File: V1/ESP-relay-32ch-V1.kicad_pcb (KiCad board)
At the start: 2 copper layers, 148 x 67.8 mm, 576 parts, among them J1 Conn_01x08, J10 USB, J11 ETHERNET, J2 Conn_01x08, J3 Conn_01x08, J4 Conn_01x08, J5 Conn_01x08, J6 Conn_01x08, J7 Conn_01x08, J8 Conn_01x08, J9 VIN, Q1 WPM2015-3/TR, Q10 MMBT2222A/SOT-23-3, Q11 MMBT2222A/SOT-23-3, Q12 MMBT2222A/SOT-23-3, Q13 MMBT2222A/SOT-23-3, Q14 MMBT2222A/SOT-23-3, Q15 MMBT2222A/SOT-23-3, Q16 MMBT2222A/SOT-23-3, Q17 MMBT2222A/SOT-23-3, Q18 MMBT2222A/SOT-23-3, Q19 MMBT2222A/SOT-23-3, Q2 LMUN2211LT1G, Q20 MMBT2222A/SOT-23-3, Q21 MMBT2222A/SOT-23-3, Q22 MMBT2222A/SOT-23-3, Q23 MMBT2222A/SOT-23-3, Q24 MMBT2222A/SOT-23-3, Q25 MMBT2222A/SOT-23-3, Q26 MMBT2222A/SOT-23-3, Q27 MMBT2222A/SOT-23-3, Q28 MMBT2222A/SOT-23-3, Q29 MMBT2222A/SOT-23-3, Q3 UMH3N, Q30 MMBT2222A/SOT-23-3, Q31 MMBT2222A/SOT-23-3, Q32 MMBT2222A/SOT-23-3, Q33 MMBT2222A/SOT-23-3, Q34 MMBT2222A/SOT-23-3, Q35 MMBT2222A/SOT-23-3, Q4 MMBT2222A/SOT-23-3, Q5 MMBT2222A/SOT-23-3, Q6 MMBT2222A/SOT-23-3, Q7 MMBT2222A/SOT-23-3, Q8 MMBT2222A/SOT-23-3, Q9 MMBT2222A/SOT-23-3, SW1 RESET, U1 SY8089A1AAC, U10 LTV-817S, U11 LTV-817S, U12 LTV-817S, U13 LTV-817S, U14 LTV-817S, U15 LTV-817S, U16 LTV-817S, U17 LTV-817S, U18 LTV-817S, U19 LTV-817S, U2 TX4138, U20 LTV-817S, U21 LTV-817S, U22 LTV-817S, U23 LTV-817S, U24 LTV-817S, U25 LTV-817S, U26 LTV-817S, U27 LTV-817S, U28 LTV-817S, U29 LTV-817S, U3 CH340C, U30 LTV-817S, U31 LTV-817S, U32 LTV-817S, U33 LTV-817S, U34 LTV-817S, U35 LTV-817S, U36 LTV-817S, U37 LTV-817S, U38 LTV-817S, U39 LTV-817S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

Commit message: Dev
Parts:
- removed the C11 at (94.6, 107.6)
- removed the C11 at (162.6, 81.4)
- removed the C12 at (162.6, 77.8)
- removed the C12 at (94.6, 101.3)
- removed the C13 at (186.1, 66.8)
- removed the C13 at (94.6, 94.9)
- removed the C14 at (184.2, 83.8)
- removed the C14 at (94.6, 88.6)
- removed the C15 at (172.5, 88.4)
- removed the C15 at (94.6, 82.2)
- removed the C16 at (198.8, 101.1)
- removed the C16 at (94.6, 75.9)
- removed the C17 at (113.7, 107.6)
- removed the C17 at (204.5, 96.7)
- removed the C18 at (113.7, 101.3)
- removed the C18 at (200.0, 100.8)
- removed the C19 at (193.4, 93.2)
- removed the C19 at (113.7, 94.9)
- removed the C20 at (201.5, 91.2)
- removed the C20 at (113.7, 88.6)
- removed the C21 at (191.3, 97.0)
- removed the C21 at (113.7, 82.2)
- removed the C22 at (113.7, 75.9)
- removed the C22 at (192.5, 97.0)
- removed the C23 at (262.1, 90.8)
- removed the C23 at (132.7, 107.6)
- removed the C25 at (262.1, 96.8)
- removed the C25 at (132.7, 94.9)
- removed the C26 at (132.7, 88.6)
- removed the C26 at (262.1, 99.9)
- removed the D10 at (279.7, 98.4)
- removed the D10 at (94.0, 114.8)
- removed the D11 at (298.6, 70.8)
- removed the D11 at (97.2, 94.1)
- removed the D12 at (298.6, 74.0)
- removed the D12 at (97.8, 114.8)
- removed the D13 at (298.6, 77.3)
- removed the D13 at (97.2, 87.8)
- removed the D14 at (101.6, 114.8)
- removed the D14 at (298.6, 80.5)
- removed the D15 at (279.7, 101.0)
- removed the D15 at (97.2, 81.4)
- removed the D16 at (279.7, 103.6)
- removed the D16 at (105.4, 114.8)
- removed the D17 at (283.8, 90.6)
- removed the D17 at (97.2, 75.1)
- removed the D18 at (109.2, 114.8)
- removed the D18 at (283.8, 93.2)
- removed the D19 at (116.2, 106.8)
- removed the D19 at (298.6, 83.8)
- removed the D20 at (113.0, 114.8)
- removed the D20 at (298.6, 87.0)
- removed the D21 at (304.9, 70.8)
- removed the D21 at (116.2, 100.5)
- removed the D22 at (116.8, 114.8)
- removed the D22 at (304.9, 74.0)
- removed the D23 at (116.2, 94.1)
- removed the D23 at (283.8, 95.8)
- removed the D24 at (283.8, 98.4)
- removed the D24 at (120.7, 114.8)
- removed the D25 at (116.2, 87.8)
- removed the D25 at (283.8, 101.0)
- removed the D26 at (124.5, 114.8)
- removed the D26 at (283.8, 103.6)
- removed the D27 at (304.9, 77.3)
- removed the D27 at (116.2, 81.4)
- removed the D28 at (128.3, 114.8)
- removed the D28 at (304.9, 80.5)
- removed the D29 at (304.9, 83.8)
- removed the D29 at (116.2, 75.1)
- removed the D30 at (132.1, 114.8)
- removed the D30 at (304.9, 87.0)
- removed the D31 at (135.3, 106.8)
- removed the D31 at (287.8, 90.6)
- removed the D32 at (287.8, 93.2)
- removed the D32 at (135.9, 114.8)
- removed the D33 at (135.3, 100.5)
- removed the D33 at (287.8, 95.8)
- removed the D34 at (287.8, 98.4)
- removed the D34 at (139.7, 114.8)
- removed the D35 at (135.3, 94.1)
- removed the D35 at (311.3, 70.8)
- removed the D36 at (311.3, 74.0)
- removed the D36 at (143.5, 114.8)
- removed the D37 at (135.3, 87.8)
- removed the D37 at (311.3, 77.3)
- removed the D6 at (160.0, 86.7)
- removed the D6 at (86.4, 114.8)
- removed the D7 at (97.2, 106.8)
- removed the D7 at (279.7, 90.6)
- removed the D8 at (279.7, 93.2)
- removed the D8 at (90.2, 114.8)
- removed the D9 at (97.2, 100.5)
- removed the D9 at (279.7, 95.8)
- removed the R10 at (86.4, 117.9)
- removed the R10 at (188.0, 68.1)
- removed the R11 at (207.3, 87.6)
- removed the R11 at (88.3, 117.3)
- removed the R12 at (110.5, 105.5)
- removed the R12 at (188.2, 83.1)
- removed the R13 at (90.2, 117.9)
- removed the R13 at (186.9, 75.4)
- removed the R14 at (188.2, 76.2)
- removed the R14 at (92.1, 117.3)
- removed the R15 at (194.9, 100.8)
- removed the R15 at (110.5, 99.2)
- removed the R16 at (183.9, 89.9)
- removed the R16 at (94.0, 117.9)
- removed the R17 at (193.4, 94.5)
- removed the R17 at (95.9, 117.3)
- removed the R18 at (196.2, 100.8)
- removed the R18 at (110.5, 92.8)
- removed the R19 at (197.5, 100.8)
- removed the R19 at (97.8, 117.9)
- removed the R20 at (193.7, 100.8)
- removed the R20 at (99.7, 117.3)
- removed the R21 at (192.4, 100.8)
- removed the R21 at (110.5, 86.5)
- removed the R22 at (203.8, 100.8)
- removed the R22 at (101.6, 117.9)
- removed the R23 at (103.5, 117.3)
- removed the R23 at (201.3, 100.8)
- removed the R24 at (110.5, 80.1)
- removed the R24 at (203.2, 96.4)
- removed the R25 at (202.6, 100.8)
- removed the R25 at (105.4, 117.9)
- removed the R26 at (193.4, 91.9)
- removed the R26 at (107.3, 117.3)
- removed the R27 at (197.1, 89.4)
- removed the R27 at (110.5, 73.8)
- removed the R28 at (199.0, 91.2)
- removed the R28 at (109.2, 117.9)
- removed the R29 at (111.1, 117.3)
- removed the R29 at (193.4, 90.7)
- removed the R30 at (193.4, 89.4)
- removed the R30 at (129.5, 105.5)
- removed the R31 at (317.9, 62.5)
- removed the R31 at (113.0, 117.9)
- removed the R32 at (317.9, 64.5)
- removed the R32 at (114.9, 117.3)
- removed the R33 at (129.5, 99.2)
- removed the R33 at (317.9, 66.5)
- removed the R34 at (317.9, 68.4)
- removed the R34 at (116.8, 117.9)
- removed the R35 at (118.7, 117.3)
- removed the R35 at (291.8, 90.6)
- removed the R36 at (291.8, 93.1)
- removed the R36 at (129.5, 92.8)
- removed the R37 at (291.8, 95.6)
- removed the R37 at (120.7, 117.9)
- removed the R38 at (122.6, 117.3)
- removed the R38 at (291.8, 98.1)
- removed the R39 at (129.5, 86.5)
- removed the R39 at (298.2, 51.1)
- removed the R40 at (298.2, 54.4)
- removed the R40 at (124.5, 117.9)
- removed the R41 at (298.2, 57.6)
- removed the R41 at (126.4, 117.3)
- removed the R42 at (298.2, 60.9)
- removed the R42 at (129.5, 80.1)
- removed the R43 at (128.3, 117.9)
- removed the R43 at (303.3, 90.3)
- removed the R44 at (130.2, 117.3)
- removed the R44 at (303.3, 92.3)
- removed the R45 at (303.3, 94.3)
- removed the R45 at (130.1, 74.3)
- removed the R46 at (303.3, 96.3)
- removed the R46 at (132.1, 117.9)
- removed the R47 at (291.8, 100.6)
- removed the R47 at (134.0, 117.3)
- removed the R48 at (148.6, 105.5)
- removed the R48 at (291.8, 103.1)
- removed the R49 at (135.9, 117.9)
- removed the R49 at (295.8, 90.6)
- removed the R50 at (295.8, 93.1)
- removed the R50 at (137.8, 117.3)
- removed the R51 at (298.2, 64.2)
- removed the R51 at (148.6, 97.9)
- removed the R52 at (139.7, 117.9)
- removed the R52 at (298.2, 67.5)
- removed the R53 at (141.6, 117.3)
- removed the R53 at (303.8, 51.1)
- removed the R54 at (303.8, 54.4)
- removed the R54 at (148.6, 92.8)
- removed the R55 at (306.2, 90.3)
- removed the R55 at (143.5, 117.9)
- removed the R56 at (306.2, 92.3)
- removed the R56 at (145.4, 117.3)
- removed the R57 at (148.6, 86.5)
- removed the R57 at (306.2, 94.3)
- removed the U10 at (123.2, 101.0)
- removed the U10 at (265.8, 52.8)
- removed the U11 at (123.2, 94.6)
- removed the U11 at (265.8, 59.4)
- removed the U12 at (265.8, 66.0)
- removed the U12 at (123.2, 88.3)
- removed the U13 at (123.2, 81.9)
- removed the U13 at (265.8, 72.7)
- removed the U14 at (265.8, 79.3)
- removed the U14 at (123.2, 75.6)
- removed U18, U19, U20, U21, U22, U23, U24, U25, U26, U27, U28, U29, U30, U31, U32, U33, U34, U35, U36, U37, U38, U39, U40, U41: LTV-817S, Tales:SMDIP-4_W9.53mm
- removed the U9 at (353.4, 55.5)
- removed the U9 at (123.2, 107.3)
- added C11: 10uF/6,3V/0603, Tales:C_0603_1608Metric, F.Cu at (156.8, 30.1)
- added C12: 0,1uF/50V/0805, Tales:C_0805_2012Metric, F.Cu at (157.0, 35.4)
- added C13: 1uF/10V/0603, Tales:C_0603_1608Metric, F.Cu at (156.8, 32.7)
- added C14: 1nF/2kV/1206, Tales:C_1206_3216Metric, F.Cu at (122.4, 43.0)
- added C15: 0,1uF/16V/0402, Tales:C_0402_1005Metric, F.Cu at (122.7, 18.4)
- added C16: 10uF/6,3V/0603, Tales:C_0603_1608Metric, F.Cu at (123.2, 30.5)
- added C17: 10uF/6,3V/0603, Tales:C_0603_1608Metric, F.Cu at (123.2, 33.0)
- added C18: 0,1uF/16V/0402, Tales:C_0402_1005Metric, F.Cu at (122.7, 20.4)
- added C19: 0,1uF/16V/0402, Tales:C_0402_1005Metric, F.Cu at (122.7, 22.4)
- added C20: 0,1uF/16V/0402, Tales:C_0402_1005Metric, F.Cu at (122.7, 24.4)
- added C21: 1uF/6,3V/0402, Tales:C_0402_1005Metric, F.Cu at (122.7, 26.3)
- added C22: 470pF/16V/0402, Tales:C_0402_1005Metric, F.Cu at (122.7, 28.3)
- added C23: 33nF/50V/0805, Tales:C_0805_2012Metric, F.Cu at (71.1, 105.7)
- added C25: 33nF/50V/0805, Tales:C_0805_2012Metric, F.Cu at (76.2, 105.7)
- added C26: 33nF/50V/0805, Tales:C_0805_2012Metric, F.Cu at (78.7, 105.7)
- added D10: BLUE/0603, Tales:LED_0603_1608Metric, F.Cu at (78.7, 117.0)
- added D11: 9V1/500mW, Tales:D_MiniMELF, F.Cu at (71.1, 100.8)
- added D12: 9V1/500mW, Tales:D_MiniMELF, F.Cu at (73.7, 100.8)
- added D13: 9V1/500mW, Tales:D_MiniMELF, F.Cu at (76.2, 100.8)
- added D14: 9V1/500mW, Tales:D_MiniMELF, F.Cu at (78.7, 100.8)
- added D15: BLUE/0603, Tales:LED_0603_1608Metric, F.Cu at (81.3, 117.0)
- added D16: BLUE/0603, Tales:LED_0603_1608Metric, F.Cu at (83.8, 117.0)
- added D17: BLUE/0603, Tales:LED_0603_1608Metric, F.Cu at (86.4, 117.0)
- added D18: BLUE/0603, Tales:LED_0603_1608Metric, F.Cu at (88.9, 117.0)
- added D19: 9V1/500mW, Tales:D_MiniMELF, F.Cu at (81.3, 100.8)
- added D20: 9V1/500mW, Tales:D_MiniMELF, F.Cu at (83.8, 100.8)
- added D21: 9V1/500mW, Tales:D_MiniMELF, F.Cu at (86.4, 100.8)
- added D22: 9V1/500mW, Tales:D_MiniMELF, F.Cu at (88.9, 100.8)
- added D23: BLUE/0603, Tales:LED_0603_1608Metric, F.Cu at (94.0, 117.0)
- added D24: BLUE/0603, Tales:LED_0603_1608Metric, F.Cu at (96.5, 117.0)
- added D25: BLUE/0603, Tales:LED_0603_1608Metric, F.Cu at (99.1, 117.0)
- added D26: BLUE/0603, Tales:LED_0603_1608Metric, F.Cu at (101.6, 117.0)
- added D27: 9V1/500mW, Tales:D_MiniMELF, F.Cu at (94.0, 100.8)
- added D28: 9V1/500mW, Tales:D_MiniMELF, F.Cu at (96.5, 100.8)
- added D29: 9V1/500mW, Tales:D_MiniMELF, F.Cu at (99.1, 100.8)
- added D30: 9V1/500mW, Tales:D_MiniMELF, F.Cu at (101.6, 100.8)
- added D31: BLUE/0603, Tales:LED_0603_1608Metric, F.Cu at (104.1, 117.0)
- added D32: BLUE/0603, Tales:LED_0603_1608Metric, F.Cu at (106.7, 117.0)
- added D33: BLUE/0603, Tales:LED_0603_1608Metric, F.Cu at (109.2, 117.0)
- added D34: BLUE/0603, Tales:LED_0603_1608Metric, F.Cu at (111.8, 117.0)
- added D35: 9V1/500mW, Tales:D_MiniMELF, F.Cu at (104.1, 100.8)
- added D36: 9V1/500mW, Tales:D_MiniMELF, F.Cu at (106.7, 100.8)
- added D37: 9V1/500mW, Tales:D_MiniMELF, F.Cu at (109.2, 100.8)
- added D6: ESDS314DBV, Package_TO_SOT_SMD:SOT-23-5, F.Cu at (122.2, 46.9)
- added D7: BLUE/0603, Tales:LED_0603_1608Metric, F.Cu at (71.1, 117.0)
- added D8: BLUE/0603, Tales:LED_0603_1608Metric, F.Cu at (73.7, 117.0)
- added D9: BLUE/0603, Tales:LED_0603_1608Metric, F.Cu at (76.2, 117.0)
- added R10: 10k/62,5mW/0402, Tales:R_0402_1005Metric, F.Cu at (153.3, 29.9)
- added R11: 10k/62,5mW/0402, Tales:R_0402_1005Metric, F.Cu at (153.3, 31.9)
- added R12: 10k/62,5mW/0402, Tales:R_0402_1005Metric, F.Cu at (153.3, 33.9)
- added R13: 3k3/62,5mW/0402, Tales:R_0402_1005Metric, F.Cu at (153.3, 35.9)
- added R14: 3k3/62,5mW/0402, Tales:R_0402_1005Metric, F.Cu at (153.3, 37.8)
- added R15: 3k3/62,5mW/0402, Tales:R_0402_1005Metric, F.Cu at (102.1, 42.3)
- added R16: 330R/62,5mW/0402, Tales:R_0402_1005Metric, F.Cu at (102.1, 44.3)
- added R17: 330R/62,5mW/0402, Tales:R_0402_1005Metric, F.Cu at (102.1, 46.3)
- added R18: 3k3/62,5mW/0402, Tales:R_0402_1005Metric, F.Cu at (102.1, 48.3)
- added R19: 3k3/62,5mW/0402, Tales:R_0402_1005Metric, F.Cu at (105.1, 42.3)
- added R20: 3k3/62,5mW/0402, Tales:R_0402_1005Metric, F.Cu at (105.1, 44.3)
- added R21: 3k3/62,5mW/0402, Tales:R_0402_1005Metric, F.Cu at (105.1, 46.3)
- added R22: 3k3/62,5mW/0402, Tales:R_0402_1005Metric, F.Cu at (105.1, 48.3)
- added R23: 3k3/62,5mW/0402, Tales:R_0402_1005Metric, F.Cu at (108.0, 42.3)
- added R24: 10k/62,5mW/0402, Tales:R_0402_1005Metric, F.Cu at (108.0, 44.3)
- added R25: 3k3/62,5mW/0402, Tales:R_0402_1005Metric, F.Cu at (108.0, 46.3)
- added R26: 12,1k/62,5mW/0402, Tales:R_0402_1005Metric, F.Cu at (108.0, 48.3)
- added R27: 49,9R/62,5mW/0402, Tales:R_0402_1005Metric, F.Cu at (110.9, 42.3)
- added R28: 49,9R/62,5mW/0402, Tales:R_0402_1005Metric, F.Cu at (110.9, 44.3)
- added R29: 49,9R/62,5mW/0402, Tales:R_0402_1005Metric, F.Cu at (110.9, 46.3)
- added R30: 49,9R/62,5mW/0402, Tales:R_0402_1005Metric, F.Cu at (110.9, 48.3)
- added R31: 1k/62,5mW/0402, Tales:R_0402_1005Metric, F.Cu at (179.8, 32.1)
- added R32: 1k/62,5mW/0402, Tales:R_0402_1005Metric, F.Cu at (179.8, 34.1)
- added R33: 1k/62,5mW/0402, Tales:R_0402_1005Metric, F.Cu at (179.8, 36.1)
- added R34: 1k/62,5mW/0402, Tales:R_0402_1005Metric, F.Cu at (179.8, 38.1)
- added R35: 5,6k/0,1W/0603, Tales:R_0603_1608Metric, F.Cu at (71.1, 113.9)
- added R36: 5,6k/0,1W/0603, Tales:R_0603_1608Metric, F.Cu at (73.7, 113.9)
- added R37: 5,6k/0,1W/0603, Tales:R_0603_1608Metric, F.Cu at (76.2, 113.9)
- added R38: 5,6k/0,1W/0603, Tales:R_0603_1608Metric, F.Cu at (78.7, 113.9)
- added R39: 1k2/0,250W/1206, Tales:R_1206_3216Metric, F.Cu at (71.1, 110.0)
- added R40: 1k2/0,250W/1206, Tales:R_1206_3216Metric, F.Cu at (73.7, 110.0)
- added R41: 1k2/0,250W/1206, Tales:R_1206_3216Metric, F.Cu at (76.2, 110.0)
- added R42: 1k2/0,250W/1206, Tales:R_1206_3216Metric, F.Cu at (78.7, 110.0)
- added R43: 3k3/62,5mW/0402, Tales:R_0402_1005Metric, F.Cu at (125.7, 130.1)
- added R44: 3k3/62,5mW/0402, Tales:R_0402_1005Metric, F.Cu at (127.0, 130.1)
- added R45: 3k3/62,5mW/0402, Tales:R_0402_1005Metric, F.Cu at (127.0, 124.0)
- added R46: 3k3/62,5mW/0402, Tales:R_0402_1005Metric, F.Cu at (125.7, 124.0)
- added R47: 5,6k/0,1W/0603, Tales:R_0603_1608Metric, F.Cu at (81.3, 113.9)
- added R48: 5,6k/0,1W/0603, Tales:R_0603_1608Metric, F.Cu at (83.8, 113.9)
- added R49: 5,6k/0,1W/0603, Tales:R_0603_1608Metric, F.Cu at (86.4, 113.9)
- added R50: 5,6k/0,1W/0603, Tales:R_0603_1608Metric, F.Cu at (88.9, 113.9)
- added R51: 1k2/0,250W/1206, Tales:R_1206_3216Metric, F.Cu at (81.3, 110.0)
- added R52: 1k2/0,250W/1206, Tales:R_1206_3216Metric, F.Cu at (83.8, 110.0)
- added R53: 1k2/0,250W/1206, Tales:R_1206_3216Metric, F.Cu at (86.4, 110.0)
- added R54: 1k2/0,250W/1206, Tales:R_1206_3216Metric, F.Cu at (88.9, 110.0)
- added R55: 3k3/62,5mW/0402, Tales:R_0402_1005Metric, F.Cu at (125.7, 121.8)
- added R56: 3k3/62,5mW/0402, Tales:R_0402_1005Metric, F.Cu at (127.0, 121.8)
- added R57: 3k3/62,5mW/0402, Tales:R_0402_1005Metric, F.Cu at (127.0, 115.7)
- added U10: OR-3H4-4, Package_SO:SOP-16_4.4x10.4mm_P1.27mm, F.Cu at (119.4, 127.0)
- added U11: OR-3H4-4, Package_SO:SOP-16_4.4x10.4mm_P1.27mm, F.Cu at (119.4, 118.8)
- added U12: OR-3H4-4, Package_SO:SOP-16_4.4x10.4mm_P1.27mm, F.Cu at (119.4, 110.5)
- added U13: OR-3H4-4, Package_SO:SOP-16_4.4x10.4mm_P1.27mm, F.Cu at (119.4, 102.3)
- added U14: OR-3H4-4, Package_SO:SOP-16_4.4x10.4mm_P1.27mm, F.Cu at (119.4, 94.0)
- added U9: MCP23017_SS, Package_SO:SSOP-28_5.3x10.2mm_P0.65mm, F.Cu at (198.3, 79.8)
- U15, U16, U17: value LTV-817S -> OR-3H4-4; footprint Tales:SMDIP-4_W9.53mm -> Package_SO:SOP-16_4.4x10.4mm_P1.27mm
- moved R87 241.9 mm to (71.1, 77.0), turned to -90 degrees
- moved R88 238.4 mm to (73.7, 77.0), turned to -90 degrees
- moved R89 234.9 mm to (76.2, 77.0), turned to -90 degrees
- moved D43 233.9 mm to (71.1, 67.8), turned to 90 degrees
- moved R101 232.9 mm to (86.4, 77.0), turned to -90 degrees
- moved R90 231.5 mm to (78.7, 77.0), turned to -90 degrees
- moved D44 230.7 mm to (73.7, 67.8), turned to 90 degrees
- moved R102 229.4 mm to (88.9, 77.0), turned to -90 degrees
- moved R99 228.0 mm to (81.3, 77.0), turned to -90 degrees
- moved D45 227.5 mm to (76.2, 67.8), turned to 90 degrees
- moved R83 225.8 mm to (71.1, 80.8), turned to -90 degrees
- moved D53 225.2 mm to (86.4, 67.8), turned to 90 degrees
- moved R100 224.6 mm to (83.8, 77.0), turned to -90 degrees
- moved D46 224.3 mm to (78.7, 67.8), turned to 90 degrees
- moved R111 223.5 mm to (94.0, 77.0), turned to -90 degrees
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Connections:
- U15 pad 1: Net-(D20-A) -> Net-(D51-A)
- U15 pad 3: GND -> Net-(D52-A)
- U15 pad 4: /GPIO Expanders/IN6 -> GND
- U16 pad 1: Net-(D21-A) -> Net-(D59-A)
- U16 pad 3: GND -> Net-(D60-A)
- U16 pad 4: /GPIO Expanders/IN7 -> GND
- U17 pad 1: Net-(D22-A) -> Net-(D67-A)
- U17 pad 3: GND -> Net-(D68-A)
- U17 pad 4: /GPIO Expanders/IN8 -> GND
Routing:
- net GND: track 733.4 -> 62.3 mm, vias 99 -> 0
- net +3.3V: track 400.9 -> 28.3 mm, vias 33 -> 0
- net +24V: track 292.4 -> 0.00 mm, vias 16 -> 0
- net /Inputs/IN1: track 162.3 -> 0.00 mm, vias 4 -> 0
- net /Inputs/IN2: track 153.6 -> 0.00 mm, vias 4 -> 0
- net /Inputs/IN3: track 140.9 -> 0.00 mm, vias 4 -> 0
- net /Inputs/IN7: track 134.0 -> 0.00 mm, vias 2 -> 0
- net /Inputs/IN4: track 123.9 -> 0.00 mm, vias 2 -> 0
- net /Inputs/IN6: track 113.4 -> 0.00 mm, vias 2 -> 0
- net /Inputs/IN5: track 108.8 -> 0.00 mm, vias 2 -> 0
- net /Inputs/IN8: track 101.5 -> 0.00 mm, vias 2 -> 0
- net +3.3VLAN: track 100.1 -> 0.00 mm, vias 4 -> 0
- net /Inputs/IN10: track 94.4 -> 0.00 mm, vias 2 -> 0
- net /Inputs/IN9: track 94.0 -> 0.00 mm, vias 2 -> 0
- net /Inputs/IN11: track 85.2 -> 0.00 mm, vias 2 -> 0
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- removed copper zone on F.Cu, net +24V
- removed copper zone on B.Cu, net +3.3V
- removed copper zone on F.Cu, net +3.3V
- removed copper zone on F.Cu, net +5V
- removed copper zone on B.Cu, net GND
- removed copper zone on F.Cu, net GND
- removed copper zone on F.Cu, net Net-(D4-K)
- removed copper zone on F.Cu, net Net-(D5-A)
- removed copper zone on B.Cu, net Net-(R4-Pad2)
- removed copper zone on F.Cu, net Net-(U1-FB)
- removed copper zone on F.Cu, net Net-(U1-LX)
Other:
- board size 148 x 67.8 mm -> 186 x 67.8 mm

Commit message: Design in course.
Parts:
- removed the C24 at (182.9, 36.5)
- J9: footprint Tales:TerminalBlock_Phoenix_PT-1,5-2-3.5-H_1x02_P3.50mm_Horizontal -> Tales:TerminalBlock_Phoenix_MKDS-3-2-5.08_1x02_P5.08mm_Horizontal
- moved C8 112.0 mm to (150.0, 127.0), turned to 180 degrees
- moved R30 95.9 mm to (186.7, 107.0)
- moved R29 95.4 mm to (186.7, 104.1)
- moved L2 95.0 mm to (161.9, 119.2), turned to 90 degrees
- moved R28 94.7 mm to (186.7, 101.0)
- moved R27 93.9 mm to (186.7, 97.8)
- moved C15 92.5 mm to (172.2, 96.5)
- moved R17 92.3 mm to (171.4, 107.3)
- moved R16 91.6 mm to (171.4, 104.1)
- moved F1 90.7 mm to (189.2, 123.2), turned to 90 degrees
- moved R1 90.4 mm to (138.9, 101.0)
- moved U2 89.7 mm to (148.0, 121.9), turned to -90 degrees
- moved R7 87.8 mm to (108.0, 21.6)
- moved R8 87.6 mm to (150.1, 128.9), turned to 180 degrees
- moved U5 87.2 mm to (179.6, 104.6)
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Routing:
- net /GPIO Expanders/OUT32: track 2.71 -> 72.9 mm, vias 0 -> 2
- net /GPIO Expanders/OUT16: track 4.23 -> 72.9 mm, vias 1 -> 2
- net /GPIO Expanders/OUT30: track 2.96 -> 63.3 mm, vias 0 -> 2
- net /GPIO Expanders/OUT14: track 4.23 -> 63.3 mm, vias 1 -> 2
- net /GPIO Expanders/OUT31: track 2.71 -> 60.7 mm, vias 0 -> 2
- net /GPIO Expanders/OUT15: track 2.71 -> 60.7 mm, vias 0 -> 2
- net /GPIO Expanders/OUT28: track 2.71 -> 53.8 mm, vias 0 -> 2
- net /GPIO Expanders/OUT12: track 4.23 -> 53.8 mm, vias 1 -> 2
- net Net-(D5-A): track 0.00 -> 49.1 mm
- net +5V: track 0.00 -> 48.1 mm, vias 0 -> 2
- net /GPIO Expanders/OUT29: track 2.71 -> 50.8 mm, vias 0 -> 2
- net /GPIO Expanders/OUT13: track 2.71 -> 50.8 mm, vias 0 -> 2
- net GND: track 62.3 -> 105.4 mm, vias 0 -> 36
- net /GPIO Expanders/OUT26: track 2.71 -> 44.2 mm, vias 0 -> 2
- net /GPIO Expanders/OUT10: track 4.28 -> 44.2 mm, vias 1 -> 2
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- added copper zone on B.Cu, net (none)
- added copper zone on F.Cu, net (none)
- added copper zone on F.Cu, net +24V
- added copper zone on F.Cu, net +3.3V
- added copper zone on F.Cu, net +5V
- added copper zone on B.Cu, net GND
- added copper zone on F.Cu, net GND
- added copper zone on F.Cu, net Net-(D4-K)
- added copper zone on F.Cu, net Net-(D5-A)
- added copper zone on F.Cu, net Net-(U1-FB)
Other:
- board text removed: "+ 24VDC -"
- board text removed: "I1"
- board text removed: "I10"
- board text removed: "I11"
- board text removed: "I12"
- board text removed: "I13"
- board text removed: "I14"
- board text removed: "I15"
- board text removed: "I16"
- board text removed: "I2"
- board text removed: "I3"
- board text removed: "I4"
- board text removed: "I5"
- board text removed: "I6"
- board text removed: "I7"
- board text removed: "I8"
- board text removed: "I9"
- board text removed: "O1"
- board text removed: "O10"
- board text removed: "O11"
- board text removed: "O12"
- board text removed: "O13"
- board text removed: "O14"
- board text removed: "O15"
- board text removed: "O16"
- board text removed: "O17"
- board text removed: "O2"
- board text removed: "O3"
- board text removed: "O4"
- board text removed: "O5"
- board text removed: "O6"
- board text removed: "O7"
- board text removed: "O8"
- board text removed: "O9"

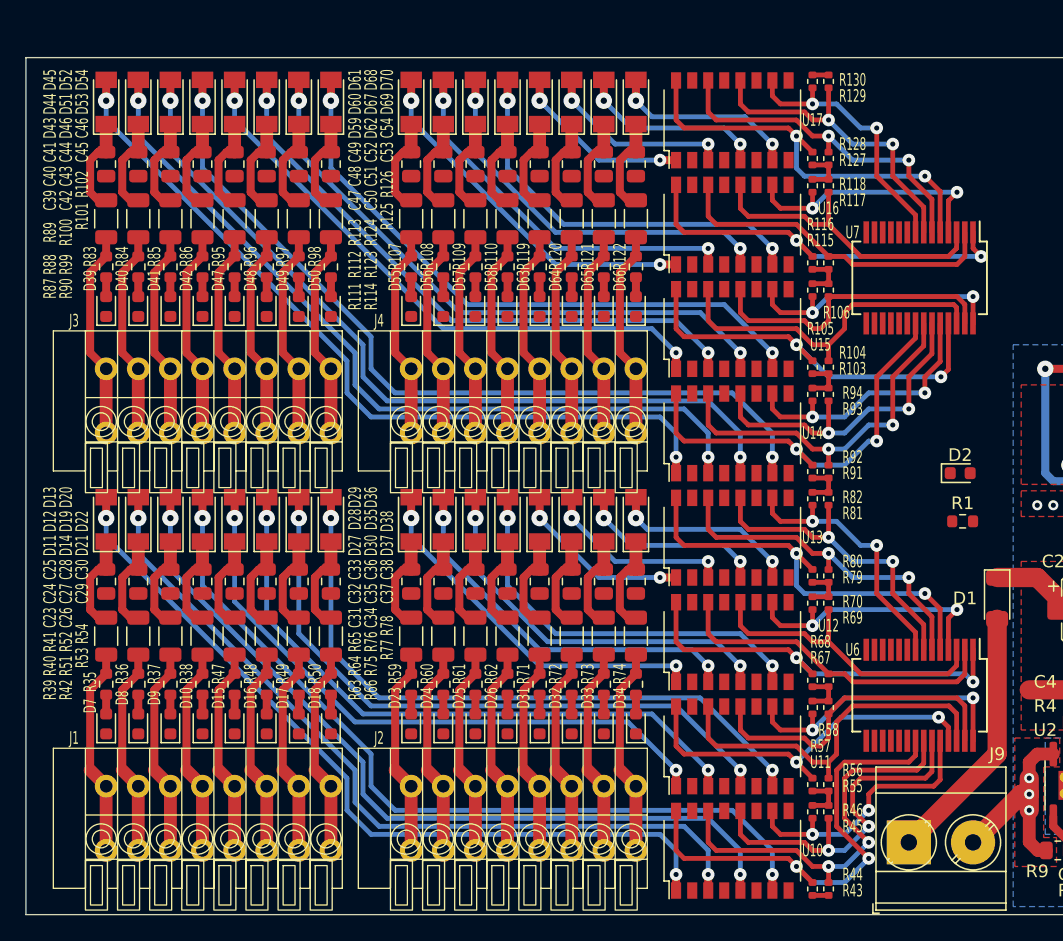
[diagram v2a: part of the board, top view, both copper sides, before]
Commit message: Update ESP-relay-32ch-V1.kicad_pcb
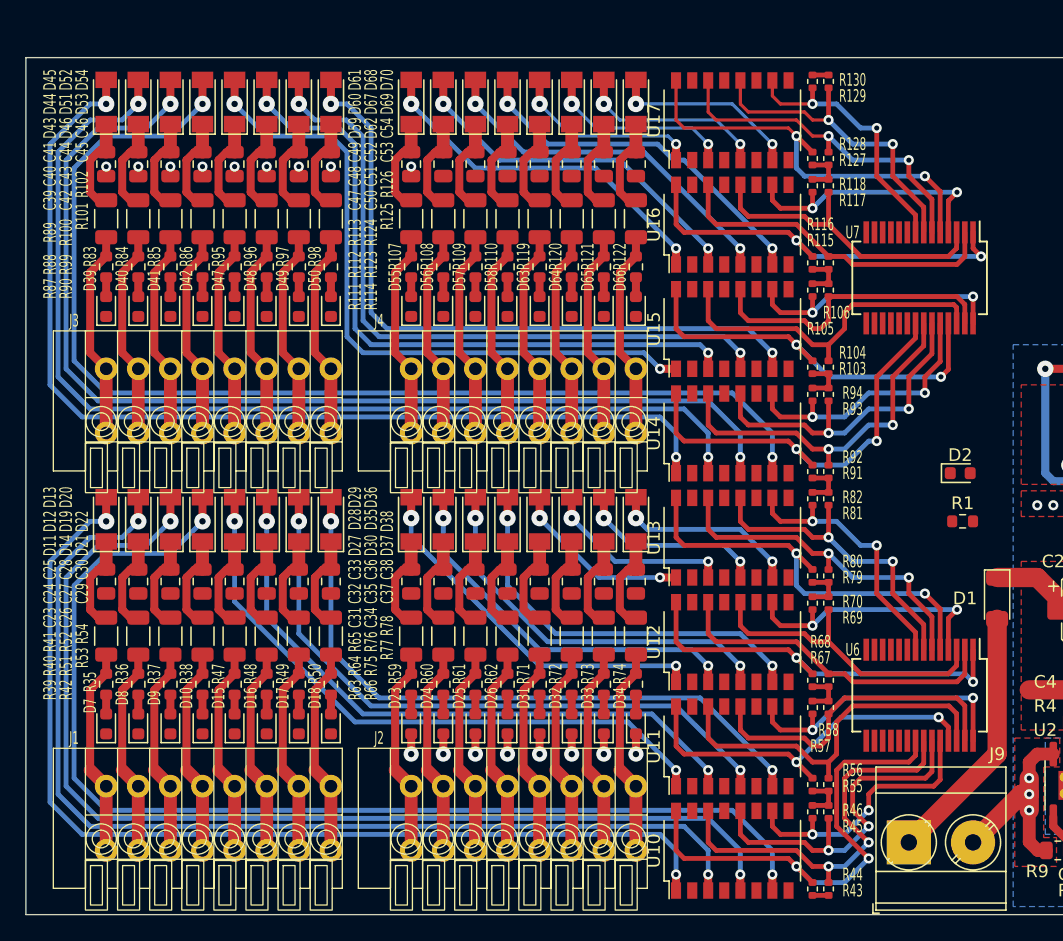
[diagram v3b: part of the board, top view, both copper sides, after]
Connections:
- C21 pad 1: Net-(#FLG06-pwr) -> (no net)
- C22 pad 1: Net-(#FLG06-pwr) -> (no net)
- U5 pad 6: Net-(#FLG06-pwr) -> (no net)
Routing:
- net Net-(D46-A): track 65.4 -> 90.2 mm
- net Net-(D14-A): track 65.4 -> 90.2 mm
- net Net-(D13-A): track 64.7 -> 87.1 mm
- net Net-(D45-A): track 64.7 -> 87.1 mm
- net Net-(D44-A): track 63.9 -> 84.1 mm
- net Net-(D12-A): track 63.9 -> 84.1 mm
- net GND: track 105.4 -> 125.0 mm, vias 36 -> 53
- net Net-(D11-A): track 63.2 -> 81.0 mm
- net Net-(D43-A): track 63.2 -> 81.0 mm
- net Net-(D51-A): track 47.0 -> 54.1 mm
- net Net-(D52-A): track 47.7 -> 54.8 mm
- net Net-(D53-A): track 48.5 -> 54.8 mm
- net Net-(D54-A): track 49.2 -> 54.8 mm
- net Net-(D62-A): track 31.8 -> 28.9 mm
- net Net-(D61-A): track 31.1 -> 28.9 mm
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
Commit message: Dev
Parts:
- D10, D100, D101, D102, D15, D16, D17, D18, D2, D23, D24, D25, D26, D31, D32, D33, D34, D39, D40, D41, D42, D47, D48, D49, D50, D55, D56, D57, D58, D63, D64, D65, D66, D7, D71, D72, D73, D74, D75, D76, D77, D78, D79, D8, D80, D81, D82, D83, D84, D85, D86, D87, D88, D89, D9, D90, D91, D92, D93, D94, D95, D96, D97, D98, D99: value BLUE/0603 -> GREEN/0603
- D11, D12, D13, D14, D19, D20, D21, D22, D27, D28, D29, D30, D35, D36, D37, D38, D43, D44, D45, D46, D51, D52, D53, D54, D59, D60, D61, D62, D67, D68, D69, D70: footprint Tales:D_MiniMELF -> Diode_SMD:D_MiniMELF
- R100, R101, R102, R111, R112, R113, R114, R123, R124, R125, R126, R39, R40, R41, R42, R51, R52, R53, R54, R63, R64, R65, R66, R75, R76, R77, R78, R87, R88, R89, R90, R99: value 1k2/0,250W/1206 -> 1k8/0,125W/0805; footprint Tales:R_1206_3216Metric -> Tales:R_0805_2012Metric
- R103, R104, R105, R106, R115, R116, R117, R118, R127, R128, R129, R13, R130, R14, R15, R18, R19, R20, R21, R22, R23, R25, R43, R44, R45, R46, R55, R56, R57, R58, R67, R68, R69, R70, R79, R80, R81, R82, R91, R92, R93, R94: value 3k3/62,5mW/0402 -> 2k2/62,5mW/0402
- U4: value ESP32-WROOM-32E-8MB -> ESP32-WROOM-32UE-N16; footprint Tales:ESP32-WROOM-32 -> Tales:ESP32-WROOM-32U
- moved R31 92.5 mm to (130.2, 117.6), turned to 90 degrees
- moved R33 85.1 mm to (195.5, 115.6)
- moved R32 61.7 mm to (130.2, 89.7), turned to 90 degrees
- moved R34 54.2 mm to (195.5, 82.5)
- moved Q3 46.0 mm to (167.3, 47.0)
- moved U3 46.0 mm to (169.5, 54.0)
- moved C11 46.0 mm to (162.6, 52.6)
- moved C12 46.0 mm to (164.5, 52.4)
- moved R67 18.0 mm to (140.3, 101.5), turned to -90 degrees
- moved R68 16.2 mm to (139.1, 101.5), turned to -90 degrees
- moved R115 15.4 mm to (140.3, 72.9), turned to -90 degrees
- moved R106 15.1 mm to (140.3, 89.7), turned to 90 degrees
- moved R58 13.5 mm to (140.3, 117.6), turned to 90 degrees
- moved R43 13.2 mm to (131.4, 117.6)
- moved R44 13.2 mm to (132.7, 117.6)
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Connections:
- C21 pad 1: (no net) -> Net-(U5-VDDCR)
- C22 pad 1: (no net) -> Net-(U5-VDDCR)
- U5 pad 6: (no net) -> Net-(U5-VDDCR)
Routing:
- net GND: track 125.0 -> 973.6 mm, vias 53 -> 136
- net +24V: track 12.5 -> 217.3 mm, vias 0 -> 16
- net /MCU/I2C_SCL: track 0.00 -> 41.4 mm
- net +3.3V: track 61.4 -> 101.6 mm, vias 2 -> 4
- net /MCU/I2C_SDA: track 0.00 -> 33.6 mm
- net Net-(D62-A): track 28.9 -> 53.8 mm
- net Net-(D30-A): track 31.8 -> 54.2 mm
- net Net-(D61-A): track 28.9 -> 50.8 mm
- net Net-(D29-A): track 31.1 -> 51.2 mm
- net Net-(D60-A): track 28.9 -> 47.7 mm
- net Net-(D28-A): track 30.4 -> 48.1 mm
- net Net-(D59-A): track 28.9 -> 43.6 mm
- net /GPIO Expanders/IN1: track 37.9 -> 23.5 mm
- net Net-(D27-A): track 29.6 -> 42.9 mm
- net /GPIO Expanders/IN17: track 33.2 -> 21.4 mm
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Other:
- board size 186 x 67.8 mm -> 194.9 x 67.8 mm

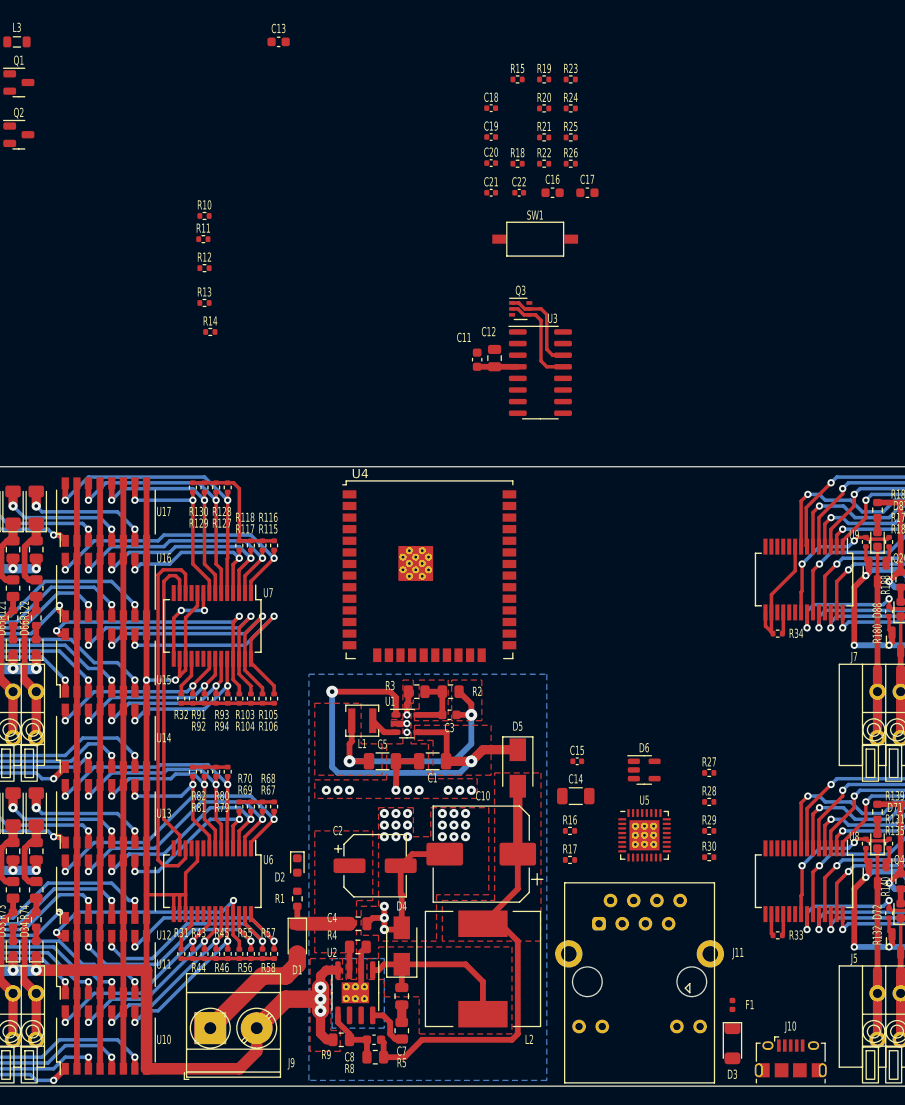
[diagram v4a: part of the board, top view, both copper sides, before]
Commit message: Update ESP-relay-32ch-V1.kicad_pcb
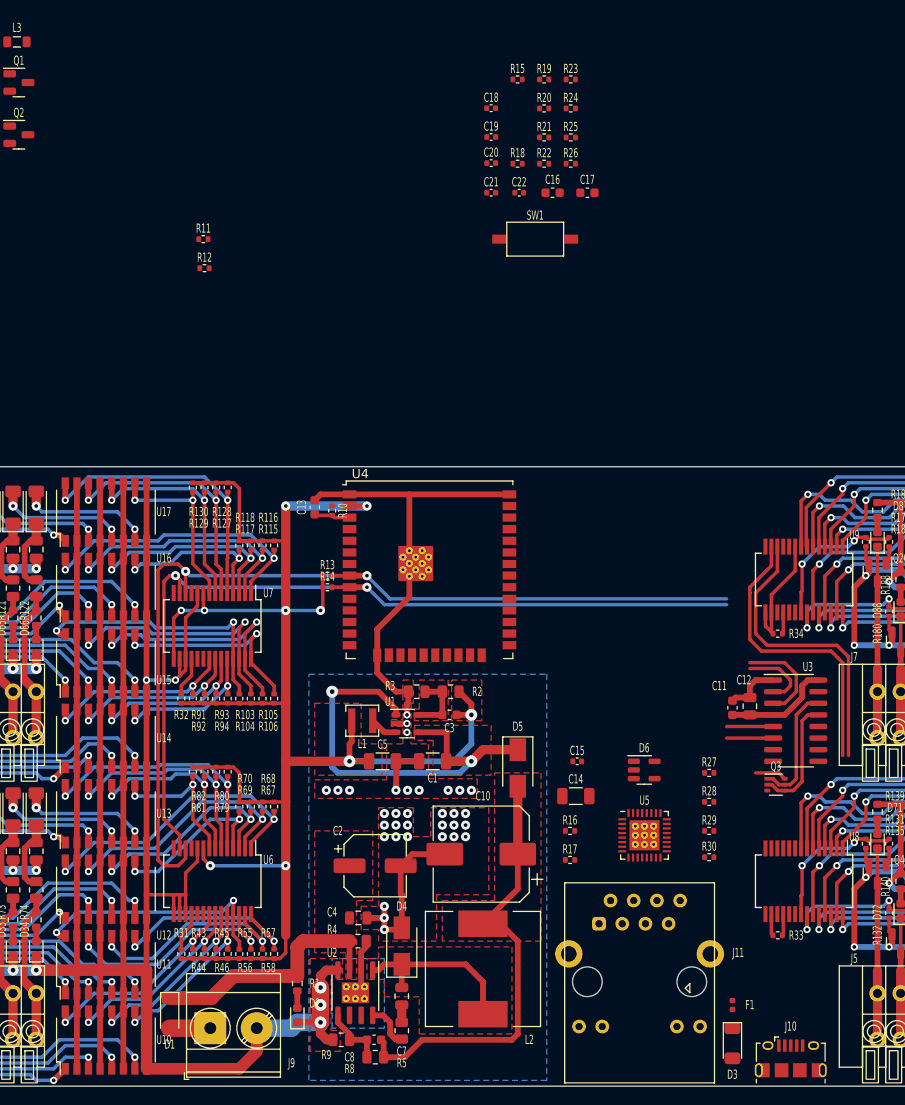
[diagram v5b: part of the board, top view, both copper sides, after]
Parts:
- moved Q3 59.1 mm to (195.3, 99.1)
- moved C13 51.1 mm to (144.8, 68.7), turned to 90 degrees
- moved C11 47.2 mm to (190.5, 90.7)
- moved C12 47.2 mm to (192.4, 90.5)
- moved U3 47.2 mm to (197.4, 92.1)
- moved R10 35.2 mm to (146.7, 69.1), turned to -90 degrees
- moved R13 32.7 mm to (146.2, 76.2)
- moved R14 30.7 mm to (146.2, 77.5)
- moved D2 16.4 mm to (142.9, 124.3), turned to 90 degrees
- moved D1 16.2 mm to (128.9, 124.1)
- moved R1 9.27 mm to (142.9, 120.8), turned to -90 degrees
- moved R4 0.64 mm to (149.5, 116.2)
- moved C4 0.63 mm to (149.5, 113.7)
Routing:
- net +3.3V: track 101.6 -> 212.0 mm, vias 4 -> 10
- net /MCU/I2C_SDA: track 33.6 -> 131.5 mm, vias 0 -> 2
- net /MCU/I2C_SCL: track 41.4 -> 139.2 mm, vias 0 -> 2
- net GND: track 973.6 -> 1026.9 mm
- net +24V: track 217.3 -> 233.8 mm
- net Net-(U3-RXD): track 0.00 -> 10.6 mm
- net Net-(D1-A): track 13.6 -> 4.44 mm
- net Net-(U3-TXD): track 0.00 -> 7.77 mm
- net Net-(Q3A-C1): track 0.00 -> 7.39 mm
- net /GPIO Expanders/IN24: track 28.4 -> 23.0 mm
- net /MCU/USB_D-: track 0.00 -> 5.08 mm
- net /MCU/USB_D+: track 0.00 -> 5.08 mm
- net Net-(Q3A-E1): track 10.2 -> 13.6 mm
- net Net-(Q3A-B1): track 10.8 -> 13.2 mm
- net Net-(D2-A): track 0.00 -> 1.85 mm
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- removed copper zone on F.Cu, net (none)
